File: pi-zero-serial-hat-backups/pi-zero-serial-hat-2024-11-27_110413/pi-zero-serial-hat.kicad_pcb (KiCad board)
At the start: 2 copper layers, 65 x 55.5 mm, 56 parts, among them J1 Conn_02x20_Counter_Clockwise, J2 Screw_Terminal_01x03, J3 Conn_01x02_Pin, J4 Conn_01x02_Pin, J5 Screw_Terminal_01x02, Q1 AOD4184, Q2 AOD4184, U1 MAX13487EESAT, U2 CX8571

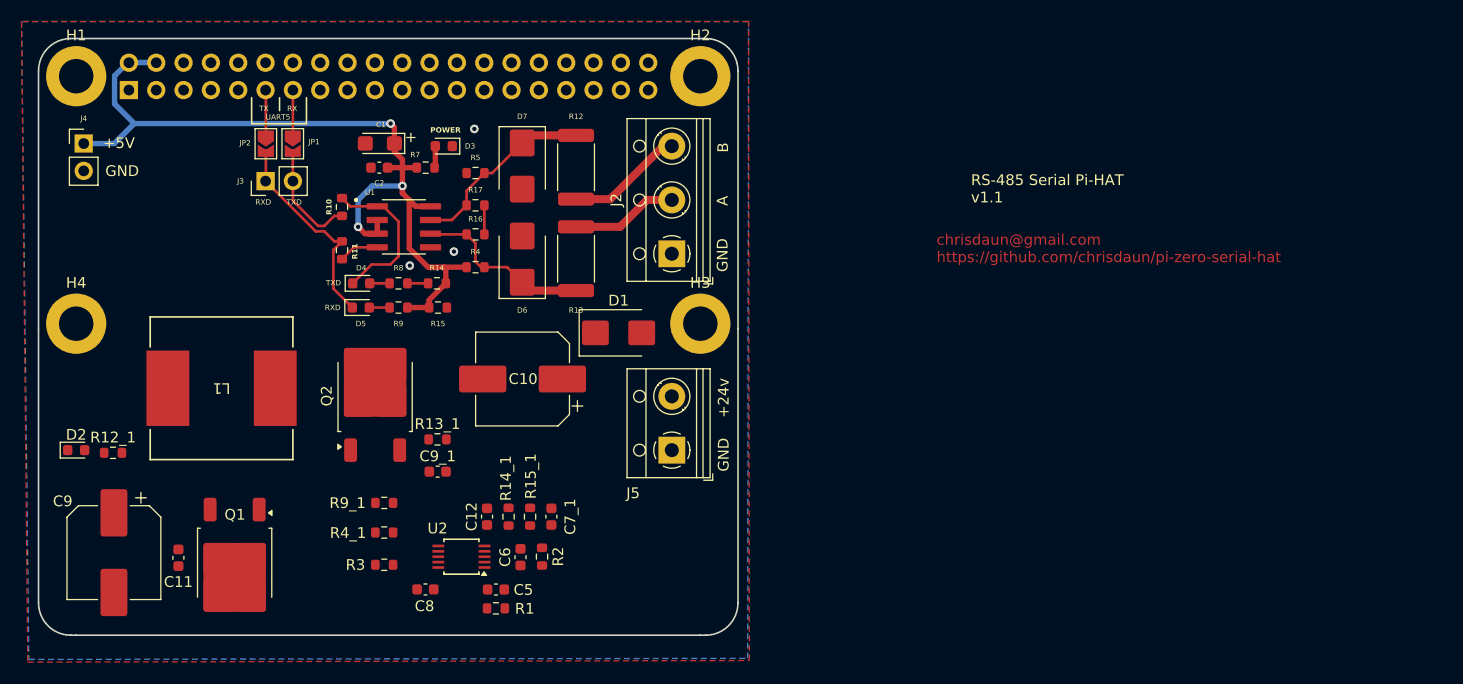
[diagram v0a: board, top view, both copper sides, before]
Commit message: Added schematic from reversed board
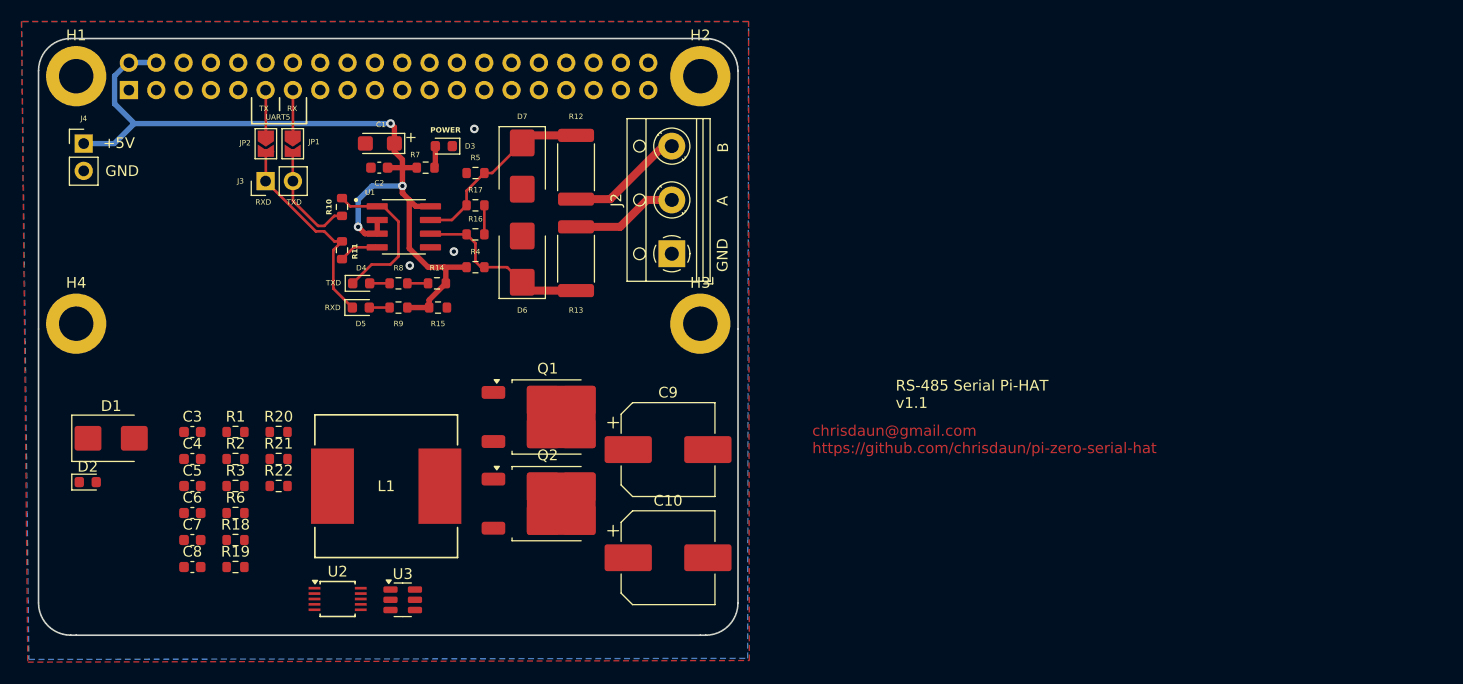
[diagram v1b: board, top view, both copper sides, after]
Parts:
- removed C11, C12, C7_1, C9_1: C, Capacitor_SMD:C_0603_1608Metric
- removed J5: Screw_Terminal_01x02, TerminalBlock_RND:TerminalBlock_RND_205-00012_1x02_P5.00mm_Horizontal
- removed R12_1: 018, Resistor_SMD:R_0603_1608Metric
- removed R13_1: 4R7, Resistor_SMD:R_0603_1608Metric
- removed R14_1, R15_1: R, Resistor_SMD:R_0603_1608Metric
- removed R4_1, R9_1: 2R2, Resistor_SMD:R_0603_1608Metric
- added C3: C, Capacitor_SMD:C_0603_1608Metric, F.Cu at (131.8, 127.6)
- added C4: C, Capacitor_SMD:C_0603_1608Metric, F.Cu at (131.8, 130.1)
- added C7: C, Capacitor_SMD:C_0603_1608Metric, F.Cu at (131.8, 137.7)
- added R18: R, Resistor_SMD:R_0603_1608Metric, F.Cu at (135.8, 137.7)
- added R19: R, Resistor_SMD:R_0603_1608Metric, F.Cu at (135.8, 140.2)
- added R20: R, Resistor_SMD:R_0603_1608Metric, F.Cu at (139.8, 127.6)
- added R21: R, Resistor_SMD:R_0603_1608Metric, F.Cu at (139.8, 130.1)
- added R22: R, Resistor_SMD:R_0603_1608Metric, F.Cu at (139.8, 132.7)
- added R6: R, Resistor_SMD:R_0603_1608Metric, F.Cu at (135.8, 135.2)
- added U3: RZC7512, Package_TO_SOT_SMD:SOT-23-6, F.Cu at (151.4, 143.2)
- C10: value 100uF 50v -> C_Polarized
- C9: value 470uF 16v -> C_Polarized
- J1: value Conn_02x20_Counter_Clockwise -> GPIO_CONNECTOR
- R1: value X10 -> R
- R2: value 473 -> R
- R3: value 4R7 -> R
- moved C9 52.4 mm to (176.0, 129.3), turned to 0 degrees
- moved D1 48.2 mm to (124.3, 128.2)
- moved Q1 32.1 mm to (164.8, 126.2), turned to 0 degrees
- moved C6 30.8 mm to (131.8, 135.2), turned to 0 degrees
- moved R2 29.9 mm to (135.8, 130.1), turned to 0 degrees
- moved C5 29.8 mm to (131.8, 132.7), turned to 0 degrees
- moved R1 29.2 mm to (135.8, 127.6)
- moved C8 21.8 mm to (131.8, 140.2)
- moved C10 21.4 mm to (176.0, 139.3), turned to 0 degrees
- moved Q2 18.9 mm to (164.8, 134.3), turned to 0 degrees
- moved L1 17.8 mm to (149.8, 132.7), turned to 0 degrees
- moved R3 15.6 mm to (135.8, 132.7)
- moved U2 12.2 mm to (145.3, 143.2), turned to 0 degrees
- moved D2 3.16 mm to (122.1, 132.3)
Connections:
- C10 pad 1: Net-(D1-K) -> unconnected-(C10-Pad1)
- C10 pad 2: GND -> unconnected-(C10-Pad2)
- C5 pad 1: GND -> unconnected-(C5-Pad1)
- C5 pad 2: Net-(U2-VIN) -> unconnected-(C5-Pad2)
- C6 pad 1: Net-(U2-COMP) -> unconnected-(C6-Pad1)
- C6 pad 2: GND -> unconnected-(C6-Pad2)
- C8 pad 1: Net-(U2-LX) -> unconnected-(C8-Pad1)
- C8 pad 2: Net-(U2-BS) -> unconnected-(C8-Pad2)
- C9 pad 1: +5V -> unconnected-(C9-Pad1)
- C9 pad 2: GND -> unconnected-(C9-Pad2)
- D1 pad 1: Net-(D1-K) -> unconnected-(D1-K-Pad1)
- D1 pad 2: +24V -> unconnected-(D1-A-Pad2)
- D2 pad 1: Net-(D2-K) -> unconnected-(D2-K-Pad1)
- D2 pad 2: +5V -> unconnected-(D2-A-Pad2)
- J1 pad 1: unconnected-(J1-Pin_1-Pad1) -> (no net)
- J1 pad 10: unconnected-(J1-Pin_10-Pad10) -> /GPIO15_RXD0
- J1 pad 11: unconnected-(J1-Pin_11-Pad11) -> GPIO17
- J1 pad 12: unconnected-(J1-Pin_12-Pad12) -> /GPIO18_GEN1
- J1 pad 13: unconnected-(J1-Pin_13-Pad13) -> GPIO27
- J1 pad 14: unconnected-(J1-Pin_14-Pad14) -> GND
- J1 pad 15: unconnected-(J1-Pin_15-Pad15) -> /GPIO22_GEN3
- J1 pad 16: unconnected-(J1-Pin_16-Pad16) -> /GPIO23_GEN4
- J1 pad 17: unconnected-(J1-Pin_17-Pad17) -> (no net)
- J1 pad 18: unconnected-(J1-Pin_18-Pad18) -> /GPIO24_GEN5
- J1 pad 19: unconnected-(J1-Pin_19-Pad19) -> /GPIO10_SPI_MOSI
- J1 pad 2: unconnected-(J1-Pin_2-Pad2) -> +5V
- J1 pad 20: unconnected-(J1-Pin_20-Pad20) -> GND
- J1 pad 21: unconnected-(J1-Pin_21-Pad21) -> /GPIO9_SPI_MISO
- J1 pad 22: unconnected-(J1-Pin_22-Pad22) -> /GPIO25_GEN6
- J1 pad 23: unconnected-(J1-Pin_23-Pad23) -> /GPIO11_SPI_SCLK
- J1 pad 24: unconnected-(J1-Pin_24-Pad24) -> /GPIO8_SPI_CE0_N
- J1 pad 25: unconnected-(J1-Pin_25-Pad25) -> GND
- J1 pad 26: unconnected-(J1-Pin_26-Pad26) -> /GPIO7_SPI_CE1_N
- J1 pad 27: unconnected-(J1-Pin_27-Pad27) -> /ID_SD
- J1 pad 28: unconnected-(J1-Pin_28-Pad28) -> /ID_SC
- J1 pad 29: unconnected-(J1-Pin_29-Pad29) -> /GPIO5
- J1 pad 3: unconnected-(J1-Pin_3-Pad3) -> /GPIO2_SDA1
- J1 pad 30: unconnected-(J1-Pin_30-Pad30) -> GND
- J1 pad 31: unconnected-(J1-Pin_31-Pad31) -> /GPIO6
- J1 pad 32: unconnected-(J1-Pin_32-Pad32) -> /GPIO12
- J1 pad 33: unconnected-(J1-Pin_33-Pad33) -> /GPIO13
- J1 pad 34: unconnected-(J1-Pin_34-Pad34) -> GND
- J1 pad 35: unconnected-(J1-Pin_35-Pad35) -> /GPIO19
- J1 pad 36: unconnected-(J1-Pin_36-Pad36) -> /GPIO16
- J1 pad 37: unconnected-(J1-Pin_37-Pad37) -> /GPIO26
- J1 pad 38: unconnected-(J1-Pin_38-Pad38) -> /GPIO20
- J1 pad 39: unconnected-(J1-Pin_39-Pad39) -> GND
- J1 pad 4: unconnected-(J1-Pin_4-Pad4) -> +5V
- J1 pad 40: unconnected-(J1-Pin_40-Pad40) -> /GPIO21
- J1 pad 5: unconnected-(J1-Pin_5-Pad5) -> /GPIO3_SCL1
- J1 pad 6: unconnected-(J1-Pin_6-Pad6) -> GND
- J1 pad 7: unconnected-(J1-Pin_7-Pad7) -> /GPIO4_GPIO_GCLK
- J1 pad 8: unconnected-(J1-Pin_8-Pad8) -> /GPIO14_TXD0
- J1 pad 9: unconnected-(J1-Pin_9-Pad9) -> GND
- L1 pad 1: Net-(Q1-S) -> Net-(L1-Pad1)
- L1 pad 2: +5V -> Net-(Q1-S)
- Q1 pad 1: Net-(Q1-G) -> unconnected-(Q1-G-Pad1)
- Q1 pad 2: Net-(D1-K) -> unconnected-(Q1-D-Pad2)
- Q2 pad 1: Net-(Q2-G) -> unconnected-(Q2-G-Pad1)
- Q2 pad 2: Net-(Q1-S) -> unconnected-(Q2-D-Pad2)
- Q2 pad 3: GND -> unconnected-(Q2-S-Pad3)
- R1 pad 1: Net-(D1-K) -> unconnected-(R1-Pad1)
- R1 pad 2: Net-(U2-VIN) -> unconnected-(R1-Pad2)
- R2 pad 1: Net-(U2-COMP) -> unconnected-(R2-Pad1)
- R2 pad 2: Net-(C7_1-Pad1) -> unconnected-(R2-Pad2)
- R3 pad 1: Net-(U2-LX) -> unconnected-(R3-Pad1)
- R3 pad 2: Net-(Q1-S) -> unconnected-(R3-Pad2)
- U2 pad 1: Net-(U2-VIN) -> unconnected-(U2-VIN-Pad1)
- U2 pad 10: Net-(U2-BS) -> unconnected-(U2-BS-Pad10)
- U2 pad 2: Net-(U2-COMP) -> unconnected-(U2-COMP-Pad2)
- U2 pad 3: Net-(U2-FB) -> unconnected-(U2-FB-Pad3)
- U2 pad 4: GND -> unconnected-(U2-SEN2-Pad4)
- U2 pad 5: GND -> unconnected-(U2-SEN1-Pad5)
- U2 pad 6: GND -> unconnected-(U2-GND-Pad6)
- U2 pad 7: Net-(U2-LG) -> unconnected-(U2-LG-Pad7)
- U2 pad 8: Net-(U2-UG) -> unconnected-(U2-UG-Pad8)
- U2 pad 9: Net-(U2-LX) -> unconnected-(U2-LX-Pad9)
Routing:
- net RXD: track 4.41 -> 0.00 mm
- net GPIO17: track 0.00 -> 4.41 mm
- net TXD: track 4.39 -> 0.00 mm
- net GPIO27: track 0.00 -> 4.39 mm
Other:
- board text removed: "+24v"
